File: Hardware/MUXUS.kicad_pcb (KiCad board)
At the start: 4 copper layers, 99.1 x 99.1 mm, 124 parts, among them J1 USB_C_Receptacle_USB2.0, J10 USB_A, J2 USB_B, J3 USB_A, J4 USB_B, J5 USB_A, J6 STDC14, J7 SWD, J8 VCP, J9 USB_B, SW1 USER, SW2 RESET, U1 USBLC6-4SC6, U10 AP2151W, U11 AOZ1212AI, U12 USBLC6-2SC6, U13 USBLC6-2SC6, U14 AP2151W, U2 USB2504A-JT, U3 USBLC6-2SC6, U4 USBLC6-2SC6, U5 AP2151W, U6 TS3USBCA420RSVR, U7 STM32G441KBU6, U8 USBLC6-2SC6, U9 USBLC6-2SC6, Y1 ATS240C

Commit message: USB, mux and 3d models update
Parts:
- J1: footprint DX07S016JA1R1500:DX07S016JA1R1500 -> USB4110-GF-A:USB4110-GF-A
- U6: value TS3USBCA420RSVR -> QFN40P180X260X55-16N
- moved C3 3.31 mm to (42.2, 17.0), turned to 180 degrees
- moved J1 3.05 mm to (33.0, 17.3)
- moved R1 1.61 mm to (42.2, 20.3), turned to 180 degrees
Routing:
- net Net-(C3-Pad2): track 8.69 -> 27.9 mm, vias 1 -> 5
- net UFP1_VBUS: track 216.3 -> 222.2 mm
- net UFP1_D-: track 37.8 -> 42.0 mm, vias 0 -> 2
- net UFP1_D+: track 34.6 -> 36.7 mm
- net GND: track 228.0 -> 229.9 mm
- net CC1: track 73.4 -> 74.1 mm

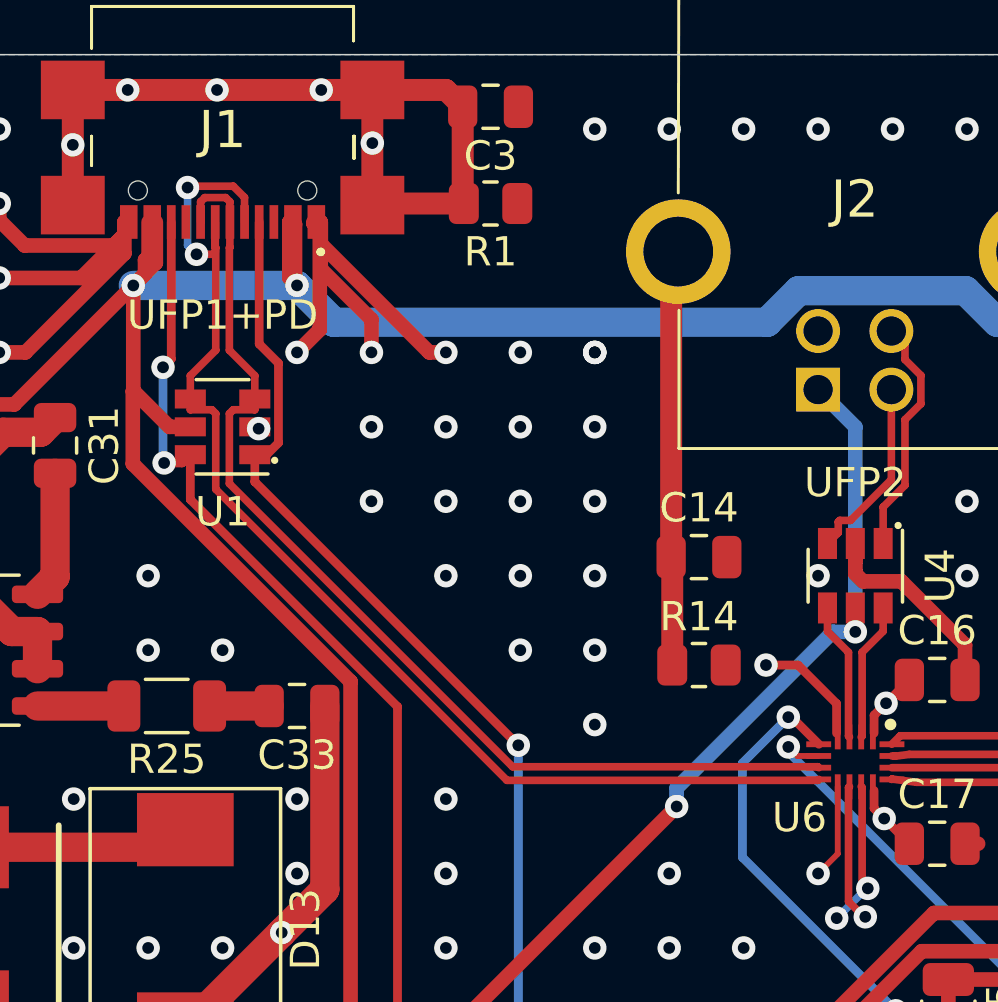
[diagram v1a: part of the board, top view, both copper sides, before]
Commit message: Update UFP1 routing
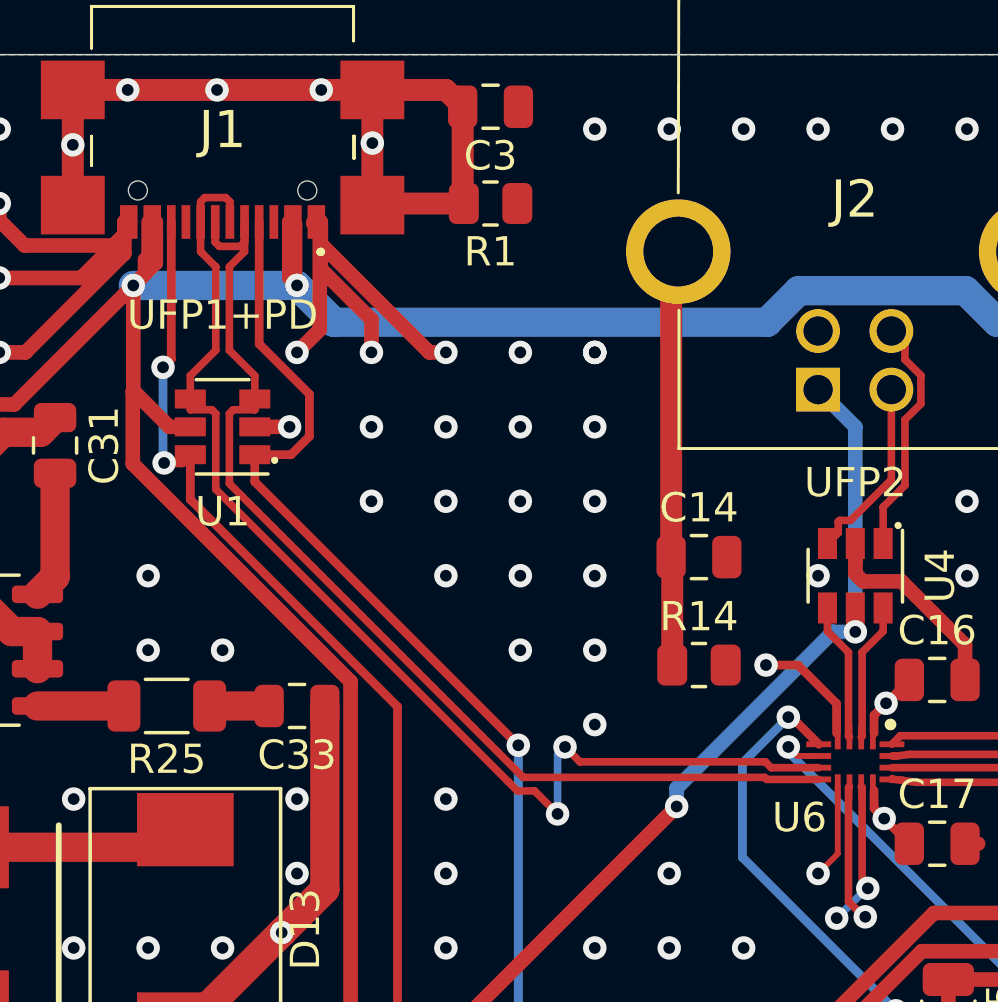
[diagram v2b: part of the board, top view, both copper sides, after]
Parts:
- U6: value QFN40P180X260X55-16N -> TS3USBCA420RSVR
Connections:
- U1 pad 3: UFP1_D+ -> UFP1_D-
- U1 pad 4: UFP1_D- -> UFP1_D+
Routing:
- net UFP1_D-: track 42.0 -> 37.1 mm, vias 2 -> 0
- net UFP1_D+: track 36.7 -> 40.6 mm, vias 0 -> 2
- net CC1: track 74.1 -> 75.5 mm
- net GND: track 229.9 -> 231.1 mm
